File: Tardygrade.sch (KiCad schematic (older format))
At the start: 25 parts, among them J1 Conn_01x03, J2 Conn_01x03, J3 Conn_01x03, J4 Conn_01x03, Q1 FET, Q2 FET, U1 MCP1642B, U2 HUZZAH32, U3 Tinypico, U4 HallSwitch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

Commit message: Changed some GPIOs. Minor edits.
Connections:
- net 3V3_Source: now also R1.1
- net HallFront: now also U2.22 (GPIO33), U3.13 (GPIO27); no longer U2.8 (GPIO39), U3.4 (GPIO5)
- net HallRear: now also U2.23 (GPIO27), U3.14 (GPIO15); no longer U2.22 (GPIO33), U3.13 (GPIO27)
- net HallRight: now also U2.24 (GPIO12), U3.15 (GPIO14); no longer U2.7 (GPIO34), U3.3 (GPIO18)
- net LidarFront: now also U2.7 (GPIO34), U3.3 (GPIO18); no longer U2.23 (GPIO27), U3.14 (GPIO15)
- net LidarRear: now also U2.8 (GPIO39), U3.4 (GPIO5); no longer U2.24 (GPIO12), U3.15 (GPIO14)
- net MOSI: now also U3.8 (GPIO33); no longer U3.7 (GPIO32)
- net PWR_EN: no longer U1.1 (EN)
- net SCK: now also U3.7 (GPIO32); no longer U3.6 (GPIO21)
- net ServoRear: now also U3.6 (GPIO21); no longer U3.8 (GPIO33)
- net VBAT_Source: no longer R1.1
- no-connect marks 1 -> 2
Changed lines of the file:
@@
 encoding utf-8
 Sheet 1 1
-Title ""
-Date ""
+Title "Tardygrade pcb v0.31"
+Date "2021-10-11"
 Rev ""
 Comp ""
@@
 Text GLabel 9750 3250 0    50   Output ~ 0
 HallLeft
-Text GLabel 5500 3200 0    50   Input ~ 0
+Text GLabel 5500 3300 0    50   Input ~ 0
 HallRear
 Text GLabel 9700 1500 0    50   Output ~ 0
 HallRear
-Text GLabel 6500 5300 2    50   Input ~ 0
+Text GLabel 5500 4900 0    50   Input ~ 0
 HallFront
-Text GLabel 6500 3500 2    50   Input ~ 0
+Text GLabel 5500 3200 0    50   Input ~ 0
 HallFront
 Text GLabel 7800 3250 0    50   Output ~ 0
 HallFront
-Text GLabel 6500 5400 2    50   Input ~ 0
+Text GLabel 5500 5100 0    50   Input ~ 0
 HallRight
-Text GLabel 6500 3600 2    50   Input ~ 0
+Text GLabel 5500 3400 0    50   Input ~ 0
 HallRight
 Text GLabel 7850 1550 0    50   Output ~ 0
@@
 Text GLabel 4850 1350 0    50   Output ~ 0
 LidarFront
-Text GLabel 5500 3300 0    50   Input ~ 0
+Text GLabel 6500 3600 2    50   Input ~ 0
 LidarFront
 $Comp
@@
 Text GLabel 1750 1500 0    50   Input ~ 0
 PWR_EN
-Text GLabel 8900 5000 0    50   Input ~ 0
-PWR_EN
 $Comp
 L power:GND #PWR0105
@@
 	0    -1   -1   0
 $EndComp
+Text GLabel 6500 5400 2    50   Input ~ 0
+LidarFront
+Text GLabel 6500 5100 2    50   Output ~ 0
+ServoRear
 Text GLabel 5500 5000 0    50   Input ~ 0
-LidarFront
-Text GLabel 6500 4900 2    50   Output ~ 0
-ServoRear
-Text GLabel 5500 4900 0    50   Input ~ 0
 HallRear
 $Comp
@@
 Text GLabel 4850 1950 0    50   Output ~ 0
 LidarRear
-Text GLabel 5500 5100 0    50   Input ~ 0
+Text GLabel 6500 5300 2    50   Input ~ 0
 LidarRear
-Text GLabel 5500 3400 0    50   Input ~ 0
+Text GLabel 6500 3500 2    50   Input ~ 0
 LidarRear
 Text GLabel 6500 3300 2    50   Output ~ 0
@@
 Text GLabel 1850 1800 0    50   UnSpc ~ 0
 3V3_Source
-Text GLabel 3250 1800 0    50   UnSpc ~ 0
-VBAT_Source
 Text GLabel 8750 4900 0    50   UnSpc ~ 0
 VBAT_Drain
@@
 Text GLabel 6500 4800 2    50   Input ~ 0
 Reset
-Text GLabel 2050 1200 1    50   UnSpc ~ 0
-VBAT_Source
 Text GLabel 3650 3400 2    50   UnSpc ~ 0
 EN
@@
 	1    0    0    -1
 $EndComp
+Text GLabel 6500 4900 2    50   UnSpc ~ 0
+MOSI
 Text GLabel 6500 5000 2    50   UnSpc ~ 0
-MOSI
-Text GLabel 6500 5100 2    50   UnSpc ~ 0
 SCK
 Text GLabel 6500 5200 2    50   UnSpc ~ 0
@@
 	6550 1800 6550 1900
 Connection ~ 6100 1800
+NoConn ~ 8900 5000
+Text GLabel 3250 1800 0    50   UnSpc ~ 0
+VBAT_Source
+Text GLabel 2050 1200 1    50   UnSpc ~ 0
+3V3_Source
 $EndSCHEMATC

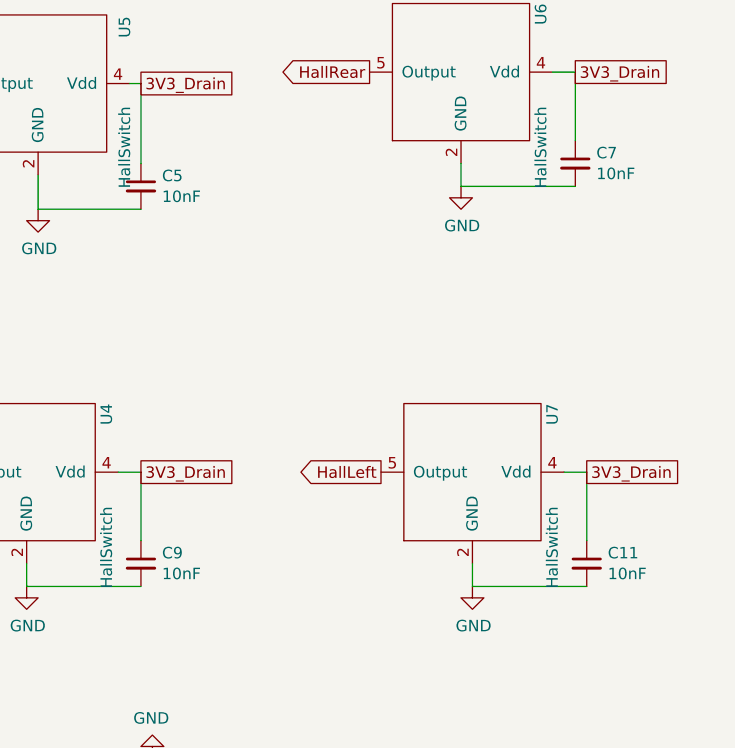
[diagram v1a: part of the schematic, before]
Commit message: Changed cap values for hall switches
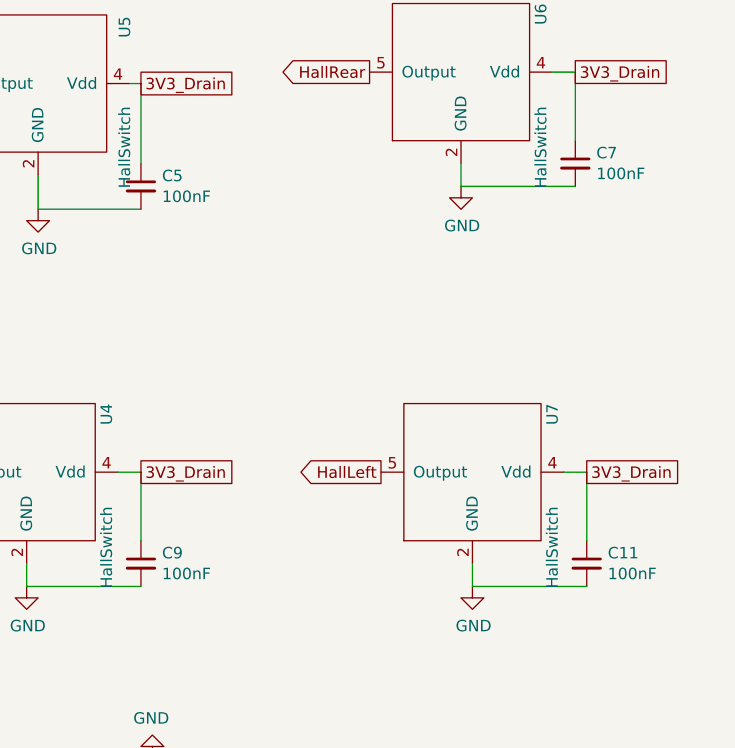
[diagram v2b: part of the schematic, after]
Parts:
- C11, C5, C7, C9: value 10nF -> 100nF
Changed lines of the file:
@@
 P 8700 3650
 F 0 "C9" H 8792 3696 50  0000 L CNN
-F 1 "10nF" H 8792 3605 50  0000 L CNN
+F 1 "100nF" H 8792 3605 50  0000 L CNN
 F 2 "Capacitor_SMD:C_0603_1608Metric_Pad1.08x0.95mm_HandSolder" H 8700 3650 50  0001 C CNN
 F 3 "~" H 8700 3650 50  0001 C CNN
@@
 P 10600 1900
 F 0 "C7" H 10692 1946 50  0000 L CNN
-F 1 "10nF" H 10692 1855 50  0000 L CNN
+F 1 "100nF" H 10692 1855 50  0000 L CNN
 F 2 "Capacitor_SMD:C_0603_1608Metric_Pad1.08x0.95mm_HandSolder" H 10600 1900 50  0001 C CNN
 F 3 "~" H 10600 1900 50  0001 C CNN
@@
 P 8700 2000
 F 0 "C5" H 8792 2046 50  0000 L CNN
-F 1 "10nF" H 8792 1955 50  0000 L CNN
+F 1 "100nF" H 8792 1955 50  0000 L CNN
 F 2 "Capacitor_SMD:C_0603_1608Metric_Pad1.08x0.95mm_HandSolder" H 8700 2000 50  0001 C CNN
 F 3 "~" H 8700 2000 50  0001 C CNN
@@
 P 10650 3650
 F 0 "C11" H 10742 3696 50  0000 L CNN
-F 1 "10nF" H 10742 3605 50  0000 L CNN
+F 1 "100nF" H 10742 3605 50  0000 L CNN
 F 2 "Capacitor_SMD:C_0603_1608Metric_Pad1.08x0.95mm_HandSolder" H 10650 3650 50  0001 C CNN
 F 3 "~" H 10650 3650 50  0001 C CNN

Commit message: v0.4 update
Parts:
- removed Q1, Q2: FET, 222footprints:SOT-23_Handsolder, symbol Transistor_FET:AO3401A
- removed R2: 200, Resistor_SMD:R_0603_1608Metric_Pad0.98x0.95mm_HandSolder, symbol Device:R
- added J5: Conn_01x03_Male, Connector_PinHeader_2.54mm:PinHeader_1x03_P2.54mm_Vertical, symbol Connector:Conn_01x03_Male
- R1: footprint Resistor_SMD:R_0603_1608Metric_Pad0.98x0.95mm_HandSolder -> Resistor_SMD:R_0201_0603Metric_Pad0.64x0.40mm_HandSolder
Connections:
- net PWR_EN is gone; now on net BOOST_EN: U2.25 (GPIO13), U3.16 (GPIO4)
- net EN: now also J5.3 (Pin_3)
- net GND: now also R1.1
- net VBAT_Drain: no longer C1.1, L1.2, U1.8 (V_IN)
- net BOOST_EN: now reaches U1.1 (EN)
- net VBAT_Rail: now reaches R1.2
- net VBAT_Rail: now also C1.1, L1.2, U1.8 (V_IN), J5.2 (Pin_2)
- net 3V3_Drain renamed 3V3_Rail
- net 3V3_Rail: now also U2.2 (3V3), U3.17 (3V3)
- removed net 3V3_Source: R1.1, U2.2 (3V3), U3.17 (3V3)
- net VBAT_Source renamed VBAT
- net VBAT: now also J5.1 (Pin_1)
- no-connect marks 2 -> 4
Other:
- moved on the sheet: C1, C2, L1, U1

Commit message: v.04 update3
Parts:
- R1: footprint Resistor_SMD:R_0201_0603Metric_Pad0.64x0.40mm_HandSolder -> Resistor_SMD:R_0603_1608Metric_Pad0.98x0.95mm_HandSolder
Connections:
- net 3V3_Rail: now also U1.1 (EN)
- net BOOST_EN: no longer U1.1 (EN)
- net EN: no longer X1.5 (B5)
- no-connect marks 4 -> 1
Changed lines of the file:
@@
 Text GLabel 6500 4800 2    50   Input ~ 0
 Reset
-Text GLabel 3650 3400 2    50   UnSpc ~ 0
-EN
 Text GLabel 3650 3600 2    50   UnSpc ~ 0
 Reset
@@
 	6550 1800 6550 1900
 Connection ~ 6100 1800
-NoConn ~ 3150 4000
-NoConn ~ 3350 4000
-NoConn ~ 3050 4000
 Text GLabel 9450 5050 0    50   Input ~ 0
-BOOST_EN
+3V3_Rail
 $Comp
 L Connector:Conn_01x03_Male J5
@@
 	9300 4550 9300 4650
 $Comp
-L power:GND #PWR?
+L power:GND #PWR0115
 U 1 1 617929C8
 P 8050 4650
-F 0 "#PWR?" H 8050 4400 50  0001 C CNN
+F 0 "#PWR0115" H 8050 4400 50  0001 C CNN
 F 1 "GND" H 8055 4477 50  0000 C CNN
 F 2 "" H 8050 4650 50  0001 C CNN
@@
 F 0 "R1" H 8120 4846 50  0000 L CNN
 F 1 "10k" H 8120 4755 50  0000 L CNN
-F 2 "Resistor_SMD:R_0201_0603Metric_Pad0.64x0.40mm_HandSolder" V 7980 4800 50  0001 C CNN
+F 2 "Resistor_SMD:R_0603_1608Metric_Pad0.98x0.95mm_HandSolder" V 7980 4800 50  0001 C CNN
 F 3 "~" H 8050 4800 50  0001 C CNN
 	1    8050 4800

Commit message: v0.4 update 4
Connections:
- net VBAT_Drain is gone; now on net SCK: X1.14 (F5)
- net 3V3_Rail: now also X1.2 (B2); no longer X1.1 (B1)
- net 5V_Rail: now also X1.3 (B3); no longer X1.12 (F7)
- net DAC1: now also X1.12 (F7); no longer X1.13 (F6)
- net GPIO21: now also X1.17 (F2); no longer X1.6 (B6)
- net GPIO36: now also X1.13 (F6); no longer X1.15 (F4)
- net MISO: now also X1.16 (F3)
- net MOSI: now also X1.15 (F4); no longer X1.17 (F2)
- net RX: now also X1.5 (B5); no longer X1.2 (B2)
- net Reset: now also X1.4 (B4); no longer X1.3 (B3)
- net SCK: no longer X1.16 (F3)
- net TX: now also X1.6 (B6); no longer X1.4 (B4)
- net VBAT_Rail: now also X1.1 (B1)
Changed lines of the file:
@@
 	1    0    0    -1
 $EndComp
-Text GLabel 3650 3800 2    50   UnSpc ~ 0
+Text GLabel 3650 3700 2    50   UnSpc ~ 0
 3V3_Rail
 $Comp
@@
 	0    1    1    0
 $EndComp
-Text GLabel 2750 3200 0    50   UnSpc ~ 0
+Text GLabel 3650 3600 2    50   UnSpc ~ 0
 5V_Rail
 Text GLabel 6500 3800 2    50   UnSpc ~ 0
@@
 Text GLabel 2750 3100 0    50   UnSpc ~ 0
 DAC2
-Text GLabel 2750 3300 0    50   UnSpc ~ 0
+Text GLabel 2750 3200 0    50   UnSpc ~ 0
 DAC1
-Text GLabel 2750 3400 0    50   UnSpc ~ 0
-VBAT_Drain
+Text GLabel 3650 3800 2    50   UnSpc ~ 0
+VBAT_Rail
 Text GLabel 6500 3400 2    50   UnSpc ~ 0
 GPIO36
@@
 Text GLabel 6500 2700 2    50   UnSpc ~ 0
 GPIO21
+Text GLabel 2750 3300 0    50   UnSpc ~ 0
+GPIO36
+Text GLabel 2750 3400 0    50   UnSpc ~ 0
+SCK
 Text GLabel 2750 3500 0    50   UnSpc ~ 0
-GPIO36
-Text GLabel 2750 3600 0    50   UnSpc ~ 0
-SCK
-Text GLabel 2750 3700 0    50   UnSpc ~ 0
 MOSI
-Text GLabel 2750 3800 0    50   UnSpc ~ 0
-MISO
 Text GLabel 5500 2700 0    50   UnSpc ~ 0
 SDA
@@
 Text GLabel 3650 3200 2    50   UnSpc ~ 0
 GPIO32
+Text GLabel 2750 3700 0    50   UnSpc ~ 0
+GPIO21
 Text GLabel 3650 3300 2    50   UnSpc ~ 0
-GPIO21
-Text GLabel 3650 3500 2    50   UnSpc ~ 0
 TX
-Text GLabel 3650 3700 2    50   UnSpc ~ 0
+Text GLabel 3650 3400 2    50   UnSpc ~ 0
 RX
 Text GLabel 6500 4800 2    50   Input ~ 0
 Reset
-Text GLabel 3650 3600 2    50   UnSpc ~ 0
+Text GLabel 3650 3500 2    50   UnSpc ~ 0
 Reset
 Text GLabel 6500 4900 2    50   UnSpc ~ 0
@@
 Text GLabel 9300 4950 0    50   UnSpc ~ 0
 VBAT_Rail
+Text GLabel 2750 3600 0    50   UnSpc ~ 0
+MISO
 $EndSCHEMATC

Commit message: v0.4 update 5
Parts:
- R1: value 10k -> 20k
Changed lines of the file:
@@
 P 8050 4800
 F 0 "R1" H 8120 4846 50  0000 L CNN
-F 1 "10k" H 8120 4755 50  0000 L CNN
+F 1 "20k" H 8120 4755 50  0000 L CNN
 F 2 "Resistor_SMD:R_0603_1608Metric_Pad0.98x0.95mm_HandSolder" V 7980 4800 50  0001 C CNN
 F 3 "~" H 8050 4800 50  0001 C CNN

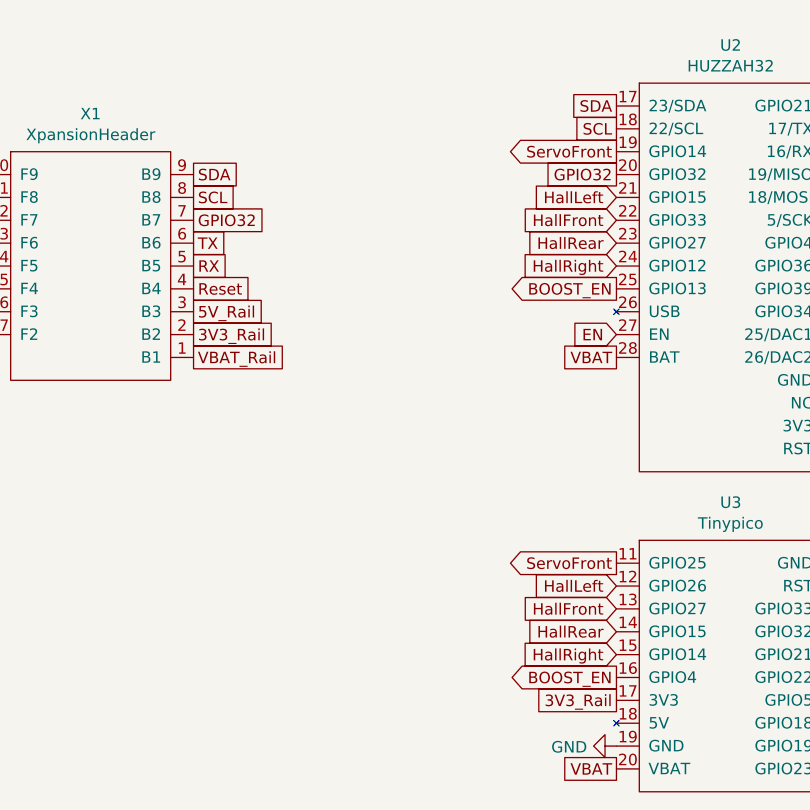
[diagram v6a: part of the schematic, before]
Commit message: Reassigned GPIO12 -> GPIO32 on Adafruit. New board v0.41
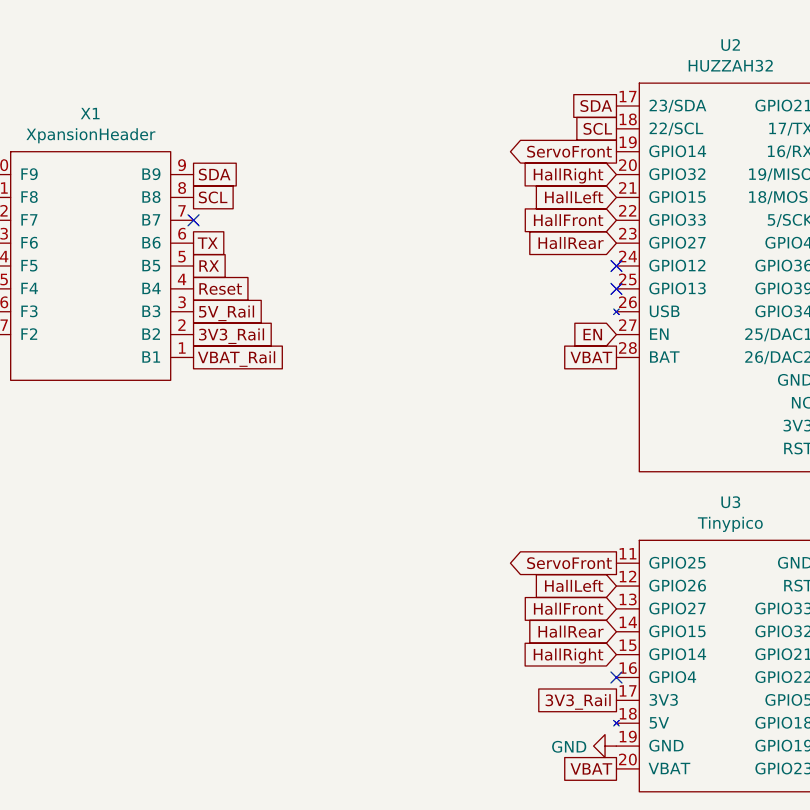
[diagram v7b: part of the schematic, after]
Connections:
- net HallRight: now also U2.20 (GPIO32); no longer U2.24 (GPIO12)
- net BOOST_EN: no longer names the net of U2.25 (GPIO13)
- net BOOST_EN: no longer U3.16 (GPIO4)
- net GPIO32: no longer names the net of X1.7 (B7)
- net GPIO32: no longer U2.20 (GPIO32)
- no-connect marks 1 -> 5
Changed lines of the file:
@@
 encoding utf-8
 Sheet 1 1
-Title "Tardygrade pcb v0.4"
-Date "2021-10-11"
+Title "Tardygrade pcb v0.41"
+Date "2021-11-21"
 Rev ""
 Comp ""
@@
 Text GLabel 5500 5100 0    50   Input ~ 0
 HallRight
-Text GLabel 5500 3400 0    50   Input ~ 0
+Text GLabel 5500 3000 0    50   Input ~ 0
 HallRight
 Text GLabel 7850 1550 0    50   Output ~ 0
@@
 Text GLabel 6100 1200 0    50   UnSpc ~ 0
 5V_Rail
-Text GLabel 5500 3500 0    50   Output ~ 0
-BOOST_EN
 Text GLabel 5500 4700 0    50   Output ~ 0
 ServoFront
@@
 Text GLabel 6500 3300 2    50   Output ~ 0
 ServoRear
-Text GLabel 5500 5200 0    50   Output ~ 0
-BOOST_EN
 Text GLabel 8200 4950 2    50   UnSpc ~ 0
 VBAT_Rail
@@
 Text GLabel 5500 2800 0    50   UnSpc ~ 0
 SCL
-Text GLabel 5500 3000 0    50   UnSpc ~ 0
-GPIO32
 Text GLabel 5500 3700 0    50   Input ~ 0
 EN
@@
 Text GLabel 3650 3100 2    50   UnSpc ~ 0
 SCL
-Text GLabel 3650 3200 2    50   UnSpc ~ 0
-GPIO32
 Text GLabel 2750 3700 0    50   UnSpc ~ 0
 GPIO21
@@
 Text GLabel 2750 3600 0    50   UnSpc ~ 0
 MISO
+NoConn ~ 5500 3500
+NoConn ~ 5500 5200
+NoConn ~ 3650 3200
+NoConn ~ 5500 3400
 $EndSCHEMATC
